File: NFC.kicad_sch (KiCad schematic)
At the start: 24 parts, among them U5 MFRC52202HN1_157, Y1 27.12MHz

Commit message: Create PCB
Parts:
- removed C14: 1uF, Capacitor_SMD:C_0603_1608Metric, symbol Device:C_Small
- removed Y1: 27.12MHz, Crystal:Crystal_HC18-U_Vertical, symbol Device:Crystal
- added C22: 1uF, Capacitor_SMD:C_0603_1608Metric, symbol Device:C_Small
- added Y1: ABM11AIG-27.120MHZ-4Z-T3, Footprints:XTAL_ABM11AIG-27.120MHZ-4Z-T3, symbol ABM11AIG-27.120MHZ-4Z-T3:ABM11AIG-27.120MHZ-4Z-T3
- Antenna1, Antenna2: footprint TestPoint:TestPoint_Pad_D4.0mm -> TestPoint:TestPoint_Pad_D2.0mm
- C15, C16, C19: DigiKey_Part_Number (none) -> 311-1445-1-ND; Manufacturer_Part_Number (none) -> CC0603KRX5R8BB105; Price (none) -> €0.95
- C17: renamed from C18; DigiKey_Part_Number (none) -> 311-1445-1-ND; Manufacturer_Part_Number (none) -> CC0603KRX5R8BB105; Price (none) -> €0.95
- C18: renamed from C17; DigiKey_Part_Number (none) -> 311-1445-1-ND; Manufacturer_Part_Number (none) -> CC0603KRX5R8BB105; Price (none) -> €0.95
- C20: renamed from C32; DigiKey_Part_Number (none) -> 311-1445-1-ND; Manufacturer_Part_Number (none) -> CC0603KRX5R8BB105; Price (none) -> €0.95
- C21: renamed from C33; DigiKey_Part_Number (none) -> 311-1445-1-ND; Manufacturer_Part_Number (none) -> CC0603KRX5R8BB105; Price (none) -> €0.95
- C23: renamed from C20; DigiKey_Part_Number (none) -> 311-1445-1-ND; Manufacturer_Part_Number (none) -> CC0603KRX5R8BB105; Price (none) -> €0.95
- C24: renamed from C21; DigiKey_Part_Number (none) -> 311-1445-1-ND; Manufacturer_Part_Number (none) -> CC0603KRX5R8BB105; Price (none) -> €0.95
- C25: renamed from C24; DigiKey_Part_Number (none) -> 311-1445-1-ND; Manufacturer_Part_Number (none) -> CC0603KRX5R8BB105; Price (none) -> €0.95
- C26: renamed from C25; DigiKey_Part_Number (none) -> 311-1445-1-ND; Manufacturer_Part_Number (none) -> CC0603KRX5R8BB105; Price (none) -> €0.95
- L2, L3: footprint Inductor_SMD:L_0603_1608Metric -> Inductor_SMD:L_1210_3225Metric; DigiKey_Part_Number (none) -> 587-3214-1-ND; Manufacturer_Part_Number (none) -> CBC3225T102KR; Price (none) -> €0.18
- R11: renamed from R10; footprint Resistor_SMD:R_0603_1608Metric -> Resistor_SMD:R_1206_3216Metric; DigiKey_Part_Number (none) -> RNCP1206FTD1K00CT-ND; Manufacturer_Part_Number (none) -> RNCP1206FTD1K00; Price (none) -> €0.70
- R12: renamed from R11; footprint Resistor_SMD:R_0603_1608Metric -> Resistor_SMD:R_1206_3216Metric; DigiKey_Part_Number (none) -> RNCP1206FTD1K00CT-ND; Manufacturer_Part_Number (none) -> RNCP1206FTD1K00; Price (none) -> €0.70
- R13: renamed from R12; footprint Resistor_SMD:R_0603_1608Metric -> Resistor_SMD:R_1206_3216Metric; DigiKey_Part_Number (none) -> RNCP1206FTD1K00CT-ND; Manufacturer_Part_Number (none) -> RNCP1206FTD1K00; Price (none) -> €0.70
- R14: renamed from R13; footprint Resistor_SMD:R_0603_1608Metric -> Resistor_SMD:R_1206_3216Metric; DigiKey_Part_Number (none) -> RNCP1206FTD1K00CT-ND; Manufacturer_Part_Number (none) -> RNCP1206FTD1K00; Price (none) -> €0.70
- R15: renamed from R14; footprint Resistor_SMD:R_0603_1608Metric -> Resistor_SMD:R_1206_3216Metric; DigiKey_Part_Number (none) -> RNCP1206FTD1K00CT-ND; Manufacturer_Part_Number (none) -> RNCP1206FTD1K00; Price (none) -> €0.70
- R16: renamed from R15; footprint Resistor_SMD:R_0603_1608Metric -> Resistor_SMD:R_1206_3216Metric; DigiKey_Part_Number (none) -> RNCP1206FTD1K00CT-ND; Manufacturer_Part_Number (none) -> RNCP1206FTD1K00; Price (none) -> €0.70
- U6: renamed from U5; value MFRC52202HN1_157 -> MFRC52202HN1_115; footprint Footprints:IC_PCAL9722HNMP -> Package_DFN_QFN:HVQFN-32-1EP_5x5mm_P0.5mm_EP3.1x3.1mm; Availability In Stock -> (none); Check_prices https://www.snapeda.com/parts/MFRC52202HN1,157/NXP+Semicond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 -> (none); Description_1 RFID Reader IC 13.56MHz ISO 14443, MIFARE I2C, SPI, UART 2.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 -> (none); DigiKey_Part_Number (none) -> 568-15200-1-ND; MF NXP USA -> (none); MP MFRC52202HN1,157 -> (none); Manufacturer NXP USA -> (none); Manufacturer_Part_Number (none) -> MFRC52202HN1,115; Package VFQFN-32 NXP Semiconductors -> (none); Price None -> €7.54; SnapEDA_Link https://www.snapeda.com/parts/MFRC52202HN1,157/NXP+Semicond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 -> (none)
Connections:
- net GND: now also C15.2, C22.2, Y1.2 (GND), Y1.4 (GND__1); no longer C15.1
- net at U6.21 (OSCIN): now also C15.1, Y1.1
- net at U6.22 (OSCOUT): now also C22.1, Y1.3; no longer C15.2

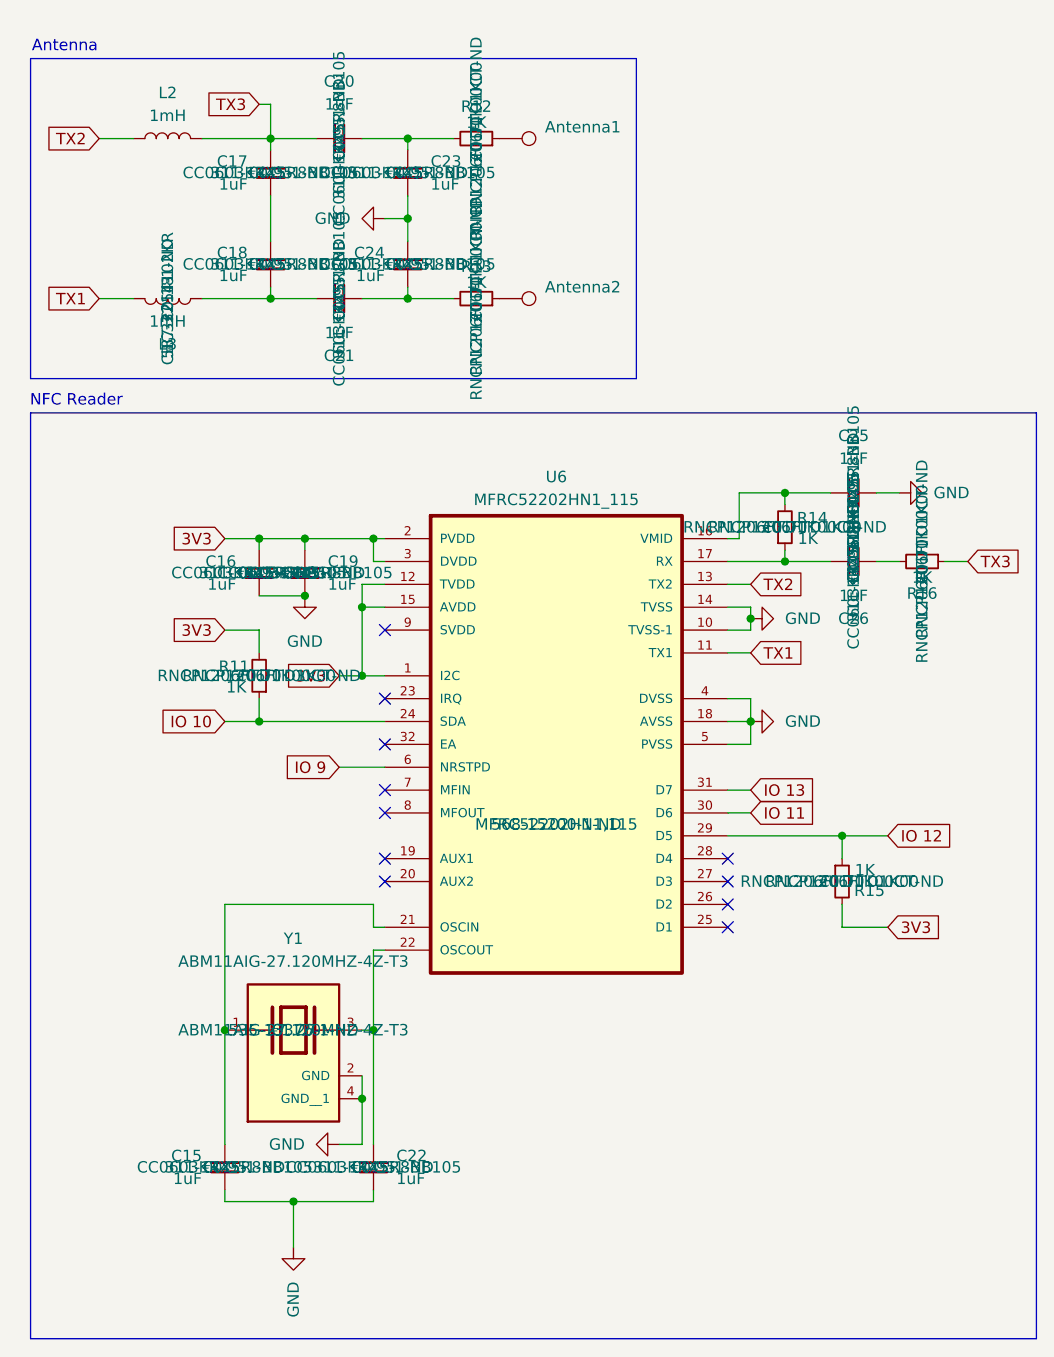
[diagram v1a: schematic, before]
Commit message: Fix minor design mistakes
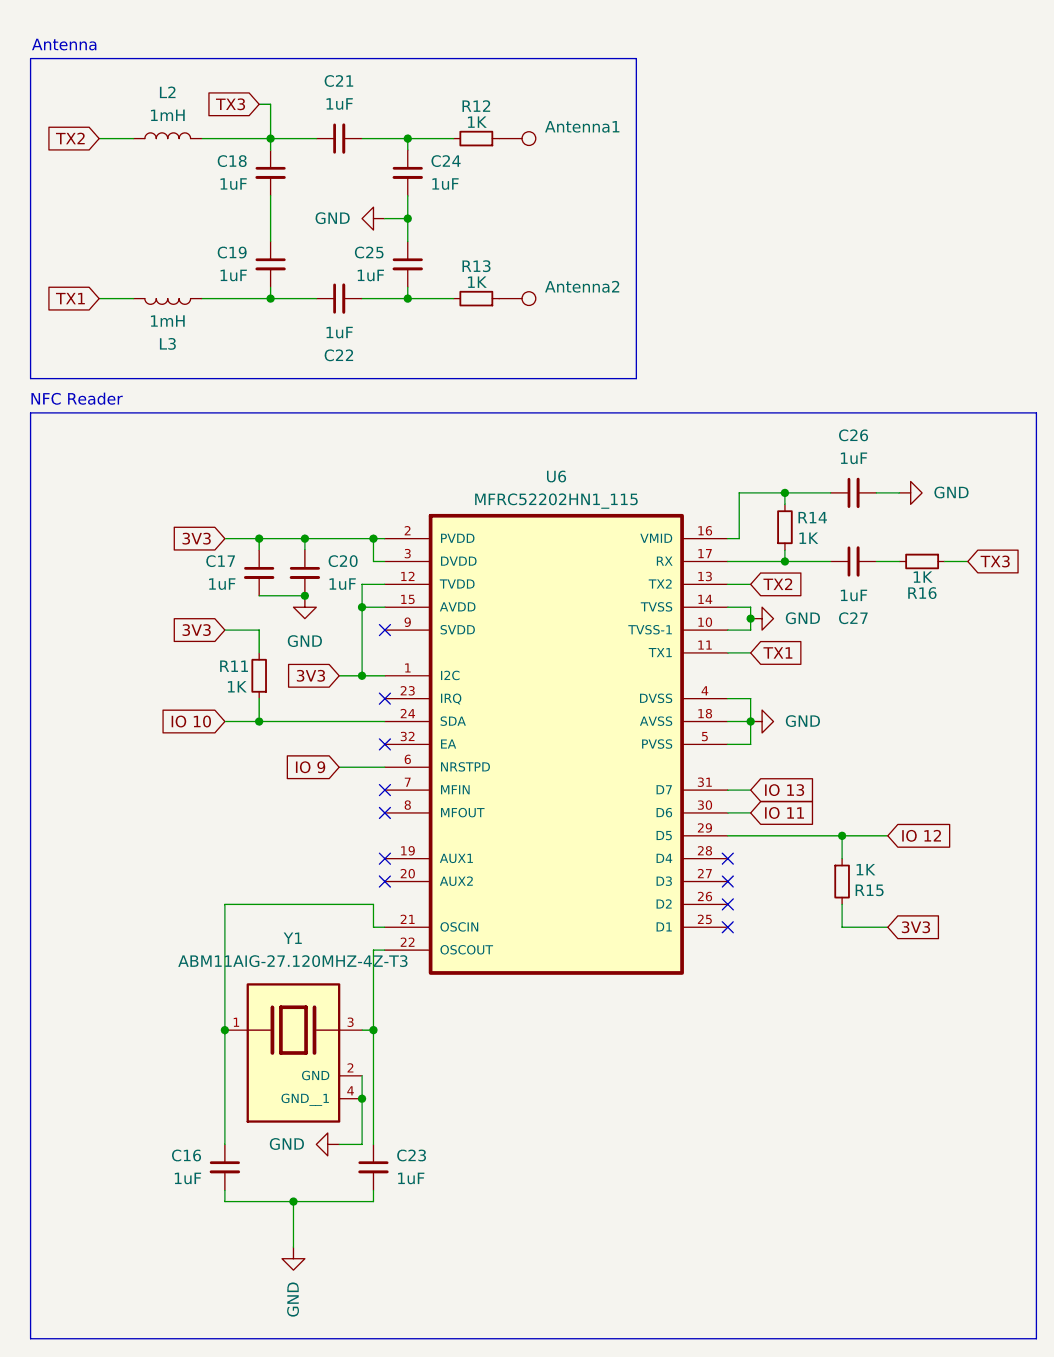
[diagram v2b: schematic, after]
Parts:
- renumbered C15 to C16, C16 to C17, C17 to C18, C18 to C19, C19 to C20, C20 to C21, C21 to C22, C22 to C23, C23 to C24, C24 to C25, C25 to C26, C26 to C27
